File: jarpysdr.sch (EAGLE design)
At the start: 40 parts

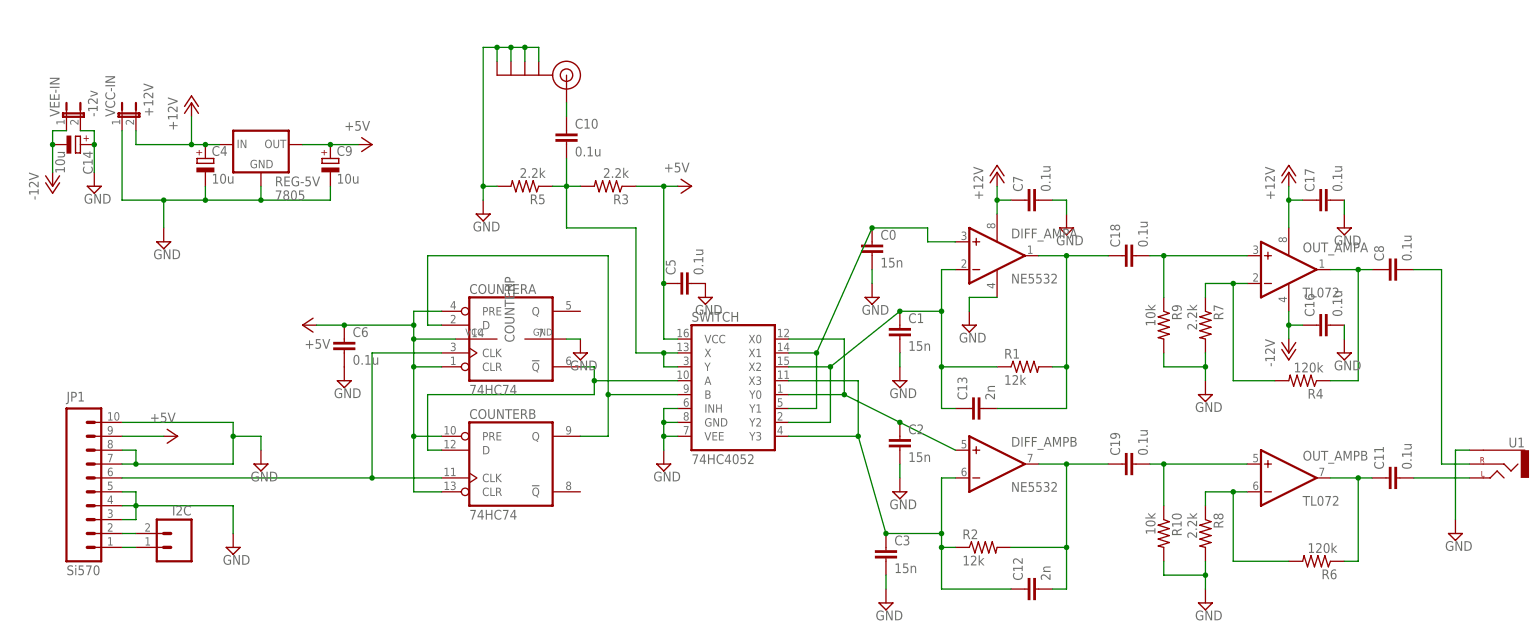
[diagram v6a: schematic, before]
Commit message: New layout. 50x50mm board.
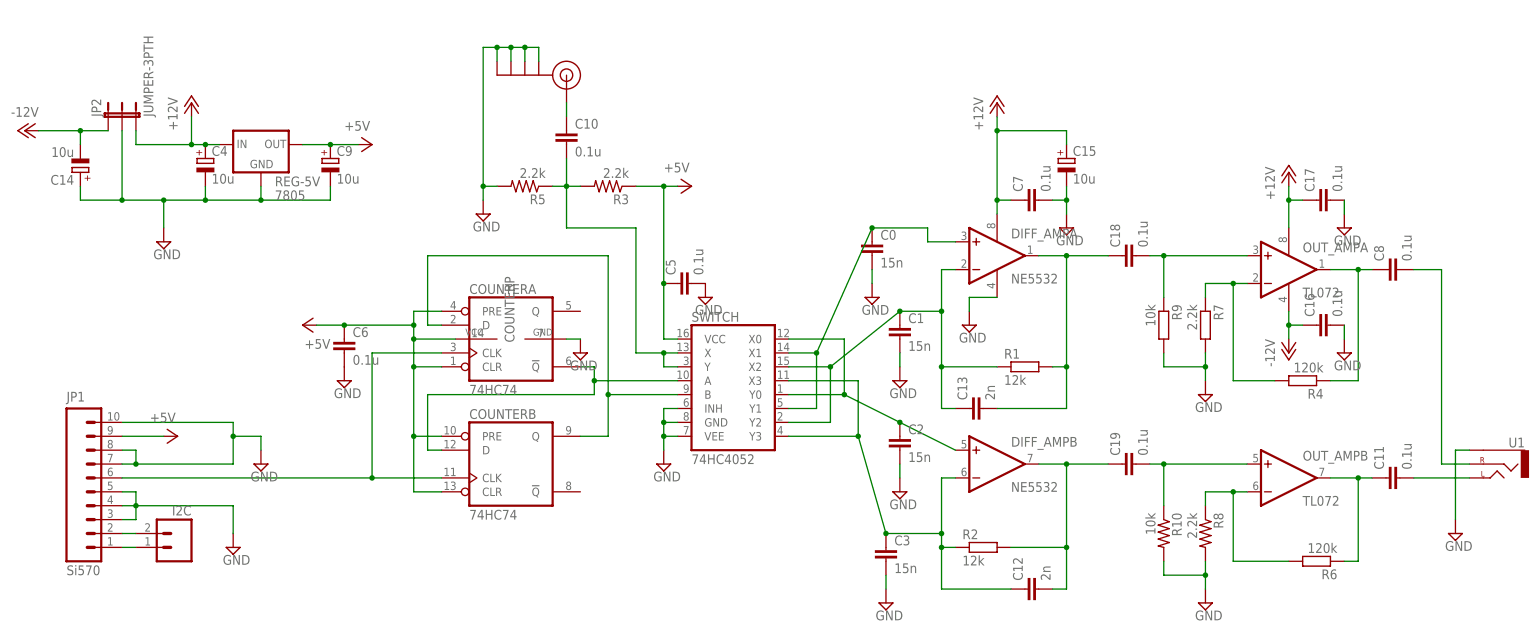
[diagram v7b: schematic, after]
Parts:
- removed VCC-IN: +12V, SparkFun:JUMPER-2PTH
- removed VEE-IN: -12v, SparkFun:JUMPER-2PTH
- added C15: 10u, resistor:CPOL-EUE2.5-6
- added JP2: JUMPER-3PTH, SparkFun:JUMPER-3PTH
- R1, R2, R4, R6, R7, R9: device resistor:R-US_0207/2V -> resistor:R-EU_0204/7
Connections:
- net +12V: now also C15.+, JP2.3; no longer VCC-IN.2
- net -12V: now also JP2.1; no longer VEE-IN.1
- net GND: now also C15.-, JP2.2; no longer VCC-IN.1, VEE-IN.2
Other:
- moved on the sheet: C14
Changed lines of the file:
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@@
 <part name="SUPPLY1" library="supply2" deviceset="GND" device=""/>
 <part name="SUPPLY2" library="supply2" deviceset="GND" device=""/>
-<part name="VCC-IN" library="SparkFun" deviceset="JUMPER-2" device="PTH" value="+12V"/>
-<part name="R1" library="resistor" deviceset="R-US_" device="0207/2V" value="12k"/>
-<part name="R2" library="resistor" deviceset="R-US_" device="0207/2V" value="12k"/>
+<part name="R1" library="resistor" deviceset="R-EU_" device="0204/7" value="12k"/>
+<part name="R2" library="resistor" deviceset="R-EU_" device="0204/7" value="12k"/>
 <part name="C0" library="resistor" deviceset="C-EU" device="025-024X044" value="15n"/>
 <part name="C1" library="resistor" deviceset="C-EU" device="025-024X044" value="15n"/>
@@
 <part name="C12" library="resistor" deviceset="C-EU" device="025-024X044" value="2n"/>
 <part name="C13" library="resistor" deviceset="C-EU" device="025-024X044" value="2n"/>
-<part name="P-2" library="supply1" deviceset="-12V" device=""/>
-<part name="VEE-IN" library="SparkFun" deviceset="JUMPER-2" device="PTH" value="-12v"/>
-<part name="SUPPLY14" library="supply2" deviceset="GND" device=""/>
 <part name="C14" library="resistor" deviceset="CPOL-EU" device="E2.5-6" value="10u"/>
 <part name="SUPPLY3" library="supply2" deviceset="GND" device=""/>
 <part name="OUT_AMP" library="linear" deviceset="TL072" device="P" value="TL072"/>
-<part name="R4" library="resistor" deviceset="R-US_" device="0207/2V" value="120k"/>
+<part name="R4" library="resistor" deviceset="R-EU_" device="0204/7" value="120k"/>
 <part name="P+2" library="supply1" deviceset="+12V" device=""/>
 <part name="P-3" library="supply1" deviceset="-12V" device=""/>
-<part name="R6" library="resistor" deviceset="R-US_" device="0207/2V" value="120k"/>
-<part name="R7" library="resistor" deviceset="R-US_" device="0207/2V" value="2.2k"/>
+<part name="R6" library="resistor" deviceset="R-EU_" device="0204/7" value="120k"/>
+<part name="R7" library="resistor" deviceset="R-EU_" device="0204/7" value="2.2k"/>
 <part name="R8" library="resistor" deviceset="R-US_" device="0204/7" value="2.2k"/>
 <part name="SUPPLY15" library="supply2" deviceset="GND" device=""/>
@@
 <part name="C18" library="resistor" deviceset="C-EU" device="050-025X075" value="0.1u"/>
 <part name="C19" library="resistor" deviceset="C-EU" device="050-025X075" value="0.1u"/>
-<part name="R9" library="resistor" deviceset="R-US_" device="0207/2V" value="10k"/>
+<part name="R9" library="resistor" deviceset="R-EU_" device="0204/7" value="10k"/>
 <part name="R10" library="resistor" deviceset="R-US_" device="0204/7" value="10k"/>
+<part name="JP2" library="SparkFun" deviceset="JUMPER-3" device="PTH"/>
+<part name="P-1" library="supply1" deviceset="-12V" device=""/>
+<part name="C15" library="resistor" deviceset="CPOL-EU" device="E2.5-6" value="10u"/>
 </parts>
 <sheets>
@@
 <instance part="SUPPLY1" gate="GND" x="-2.54" y="27.94"/>
 <instance part="SUPPLY2" gate="GND" x="76.2" y="43.18"/>
-<instance part="VCC-IN" gate="A" x="-22.86" y="106.68"/>
 <instance part="R1" gate="G$1" x="142.24" y="60.96"/>
 <instance part="R2" gate="G$1" x="134.62" y="27.94"/>
@@
 <instance part="DIFF_AMP" gate="B" x="137.16" y="43.18"/>
 <instance part="DIFF_AMP" gate="P" x="137.16" y="81.28"/>
-<instance part="P+1" gate="1" x="137.16" y="96.52"/>
+<instance part="P+1" gate="1" x="137.16" y="109.22"/>
 <instance part="C7" gate="G$1" x="142.24" y="91.44" rot="R90"/>
 <instance part="SUPPLY6" gate="GND" x="149.86" y="86.36"/>
@@
 <instance part="C12" gate="G$1" x="142.24" y="20.32" rot="R90"/>
 <instance part="C13" gate="G$1" x="132.08" y="53.34" rot="R90"/>
-<instance part="P-2" gate="1" x="-35.56" y="93.98"/>
-<instance part="VEE-IN" gate="A" x="-33.02" y="106.68"/>
-<instance part="SUPPLY14" gate="GND" x="-27.94" y="93.98"/>
-<instance part="C14" gate="G$1" x="-30.48" y="101.6" rot="R270"/>
+<instance part="C14" gate="G$1" x="-30.48" y="96.52" rot="R180"/>
 <instance part="SUPPLY3" gate="GND" x="132.08" y="68.58"/>
 <instance part="OUT_AMP" gate="A" x="190.5" y="78.74"/>
@@
 <instance part="R9" gate="G$1" x="167.64" y="68.58" rot="R270"/>
 <instance part="R10" gate="G$1" x="167.64" y="30.48" rot="R270"/>
+<instance part="JP2" gate="G$1" x="-25.4" y="106.68"/>
+<instance part="P-1" gate="1" x="-40.64" y="104.14" rot="R270"/>
+<instance part="C15" gate="G$1" x="149.86" y="99.06"/>
 </instances>
 <busses>
@@
 <wire x1="2.54" y1="91.44" x2="-7.62" y2="91.44" width="0.1524" layer="91"/>
 <wire x1="-7.62" y1="91.44" x2="-15.24" y2="91.44" width="0.1524" layer="91"/>
-<wire x1="-22.86" y1="104.14" x2="-22.86" y2="91.44" width="0.1524" layer="91"/>
-<wire x1="-22.86" y1="91.44" x2="-15.24" y2="91.44" width="0.1524" layer="91"/>
 <wire x1="-7.62" y1="91.44" x2="-7.62" y2="93.98" width="0.1524" layer="91"/>
 <wire x1="15.24" y1="93.98" x2="15.24" y2="91.44" width="0.1524" layer="91"/>
@@
 <pinref part="SUPPLY4" gate="GND" pin="GND"/>
 <pinref part="REG-5V" gate="1" pin="GND"/>
-<pinref part="VCC-IN" gate="A" pin="1"/>
 <pinref part="C4" gate="G$1" pin="-"/>
 <pinref part="C9" gate="G$1" pin="-"/>
+<wire x1="-30.48" y1="91.44" x2="-22.86" y2="91.44" width="0.1524" layer="91"/>
+<pinref part="C14" gate="G$1" pin="+"/>
+<wire x1="-22.86" y1="91.44" x2="-15.24" y2="91.44" width="0.1524" layer="91"/>
+<wire x1="-30.48" y1="93.98" x2="-30.48" y2="91.44" width="0.1524" layer="91"/>
+<pinref part="JP2" gate="G$1" pin="2"/>
+<wire x1="-22.86" y1="104.14" x2="-22.86" y2="91.44" width="0.1524" layer="91"/>
+<junction x="-22.86" y="91.44"/>
 </segment>
 <segment>
@@
 <pinref part="C7" gate="G$1" pin="2"/>
 <pinref part="SUPPLY6" gate="GND" pin="GND"/>
+<pinref part="C15" gate="G$1" pin="-"/>
+<wire x1="149.86" y1="93.98" x2="149.86" y2="91.44" width="0.1524" layer="91"/>
+<junction x="149.86" y="91.44"/>
 </segment>
 <segment>
@@
 <pinref part="COUNTER" gate="P" pin="GND"/>
 <pinref part="SUPPLY13" gate="GND" pin="GND"/>
-</segment>
-<segment>
-<wire x1="-30.48" y1="104.14" x2="-27.94" y2="104.14" width="0.1524" layer="91"/>
-<wire x1="-27.94" y1="104.14" x2="-27.94" y2="101.6" width="0.1524" layer="91"/>
-<wire x1="-27.94" y1="101.6" x2="-27.94" y2="96.52" width="0.1524" layer="91"/>
-<junction x="-27.94" y="101.6"/>
-<pinref part="VEE-IN" gate="A" pin="2"/>
-<pinref part="SUPPLY14" gate="GND" pin="GND"/>
-<pinref part="C14" gate="G$1" pin="+"/>
 </segment>
 <segment>
@@
 <net name="+12V" class="0">
 <segment>
-<wire x1="-20.32" y1="104.14" x2="-20.32" y2="101.6" width="0.1524" layer="91"/>
 <wire x1="-20.32" y1="101.6" x2="-10.16" y2="101.6" width="0.1524" layer="91"/>
 <wire x1="-10.16" y1="101.6" x2="-7.62" y2="101.6" width="0.1524" layer="91"/>
@@
 <junction x="-10.16" y="101.6"/>
 <junction x="-7.62" y="101.6"/>
-<pinref part="VCC-IN" gate="A" pin="2"/>
 <pinref part="REG-5V" gate="1" pin="IN"/>
 <pinref part="P+7" gate="1" pin="+12V"/>
 <pinref part="C4" gate="G$1" pin="+"/>
+<pinref part="JP2" gate="G$1" pin="3"/>
+<wire x1="-20.32" y1="104.14" x2="-20.32" y2="101.6" width="0.1524" layer="91"/>
 </segment>
 <segment>
 <wire x1="137.16" y1="88.9" x2="137.16" y2="91.44" width="0.1524" layer="91"/>
-<wire x1="137.16" y1="91.44" x2="137.16" y2="93.98" width="0.1524" layer="91"/>
+<wire x1="137.16" y1="91.44" x2="137.16" y2="104.14" width="0.1524" layer="91"/>
+<wire x1="137.16" y1="104.14" x2="137.16" y2="106.68" width="0.1524" layer="91"/>
 <wire x1="139.7" y1="91.44" x2="137.16" y2="91.44" width="0.1524" layer="91"/>
 <junction x="137.16" y="91.44"/>
@@
 <pinref part="P+1" gate="1" pin="+12V"/>
 <pinref part="C7" gate="G$1" pin="1"/>
+<pinref part="C15" gate="G$1" pin="+"/>
+<wire x1="149.86" y1="101.6" x2="149.86" y2="104.14" width="0.1524" layer="91"/>
+<wire x1="149.86" y1="104.14" x2="137.16" y2="104.14" width="0.1524" layer="91"/>
+<junction x="137.16" y="104.14"/>
 </segment>
 <segment>
@@
 <net name="-12V" class="0">
 <segment>
-<wire x1="-33.02" y1="104.14" x2="-35.56" y2="104.14" width="0.1524" layer="91"/>
-<wire x1="-35.56" y1="104.14" x2="-35.56" y2="101.6" width="0.1524" layer="91"/>
-<wire x1="-35.56" y1="101.6" x2="-35.56" y2="96.52" width="0.1524" layer="91"/>
-<junction x="-35.56" y="101.6"/>
-<pinref part="VEE-IN" gate="A" pin="1"/>
-<pinref part="P-2" gate="1" pin="-12V"/>
-<pinref part="C14" gate="G$1" pin="-"/>
-</segment>
-<segment>
 <wire x1="190.5" y1="71.12" x2="190.5" y2="68.58" width="0.1524" layer="91"/>
 <wire x1="190.5" y1="68.58" x2="190.5" y2="66.04" width="0.1524" layer="91"/>
@@
 <pinref part="C16" gate="G$1" pin="1"/>
 </segment>
-</net>
+<segment>
+<pinref part="JP2" gate="G$1" pin="1"/>
+<wire x1="-25.4" y1="104.14" x2="-30.48" y2="104.14" width="0.1524" layer="91"/>
+<pinref part="C14" gate="G$1" pin="-"/>
+<wire x1="-30.48" y1="104.14" x2="-30.48" y2="101.6" width="0.1524" layer="91"/>
+<pinref part="P-1" gate="1" pin="-12V"/>
+<wire x1="-38.1" y1="104.14" x2="-30.48" y2="104.14" width="0.1524" layer="91"/>
+<junction x="-30.48" y="104.14"/>
+</segment>
+</net>
